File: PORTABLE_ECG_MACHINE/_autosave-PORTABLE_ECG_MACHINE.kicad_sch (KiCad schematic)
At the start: 55 parts, among them IC1 AD8232ACPZ, J1 USB_B_Micro, J2 Li-Ion 3.7 CONN, J3 UART, Q1 BSS138, Q2 BSS138, SW1 SW_SPDT, U1 CP2102-GM, U2 TP4056, U3 TC1262-33, U4 SSD1306

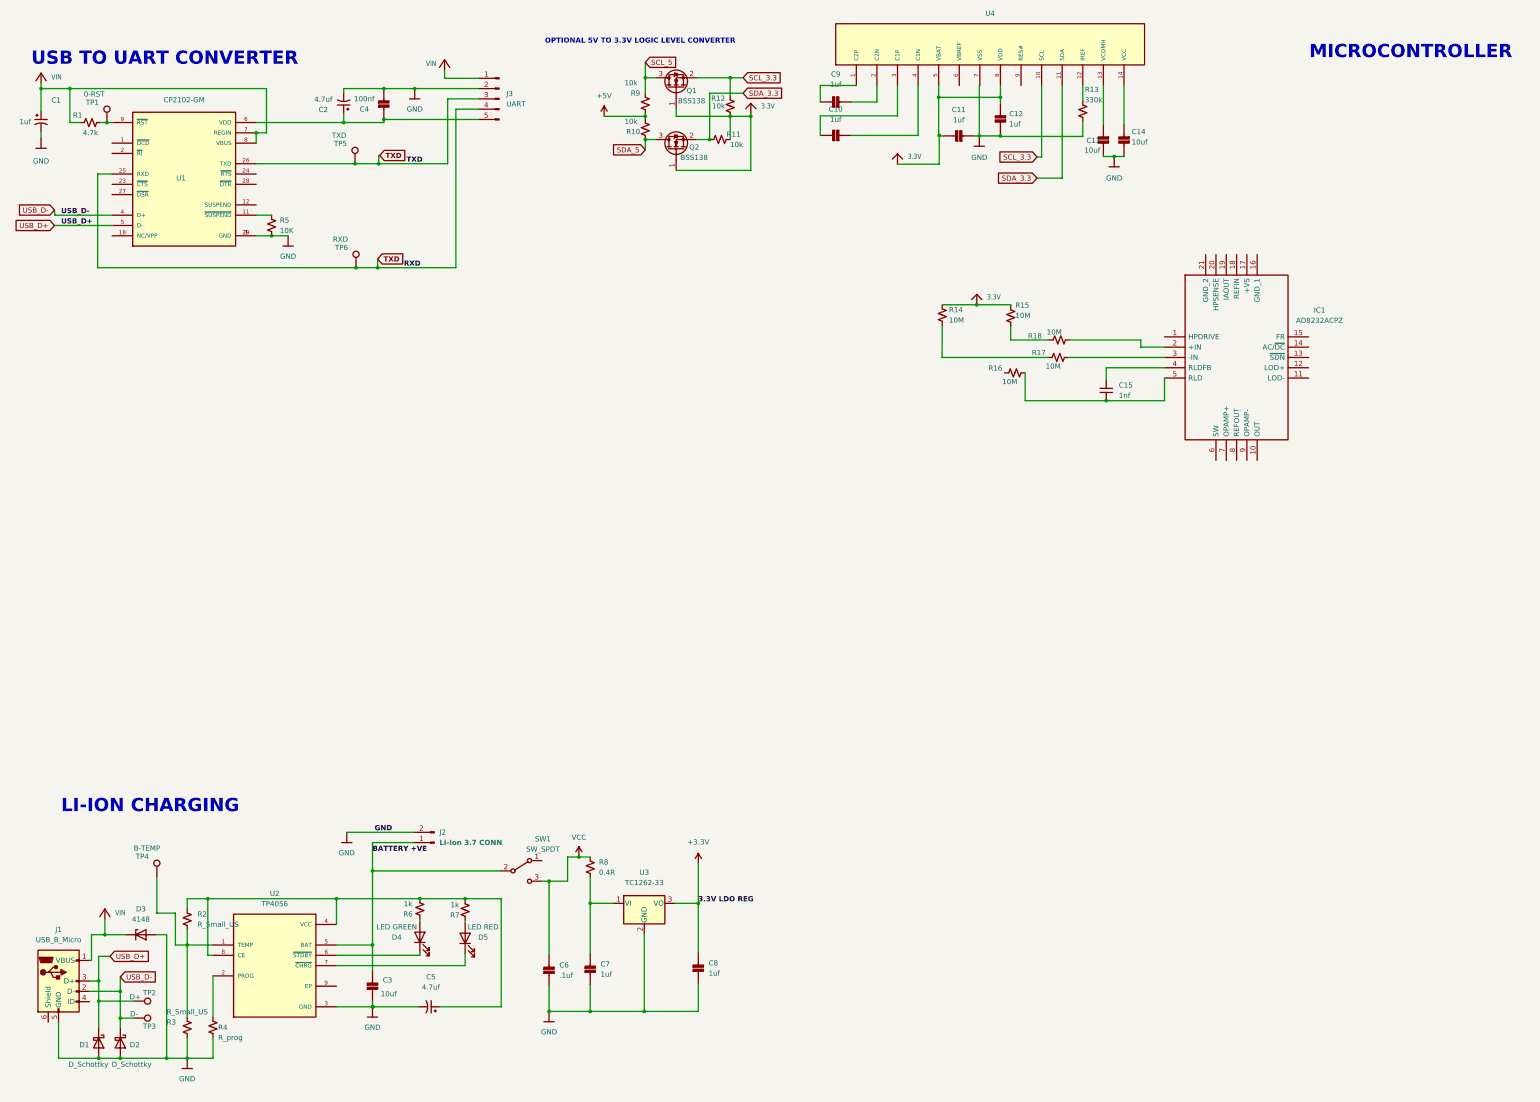
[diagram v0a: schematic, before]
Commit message: OLED-INSTR_AMP-LION_CHAR-UART EESCHEMA UPDATE | PCBNEW ROUGH ARANGE
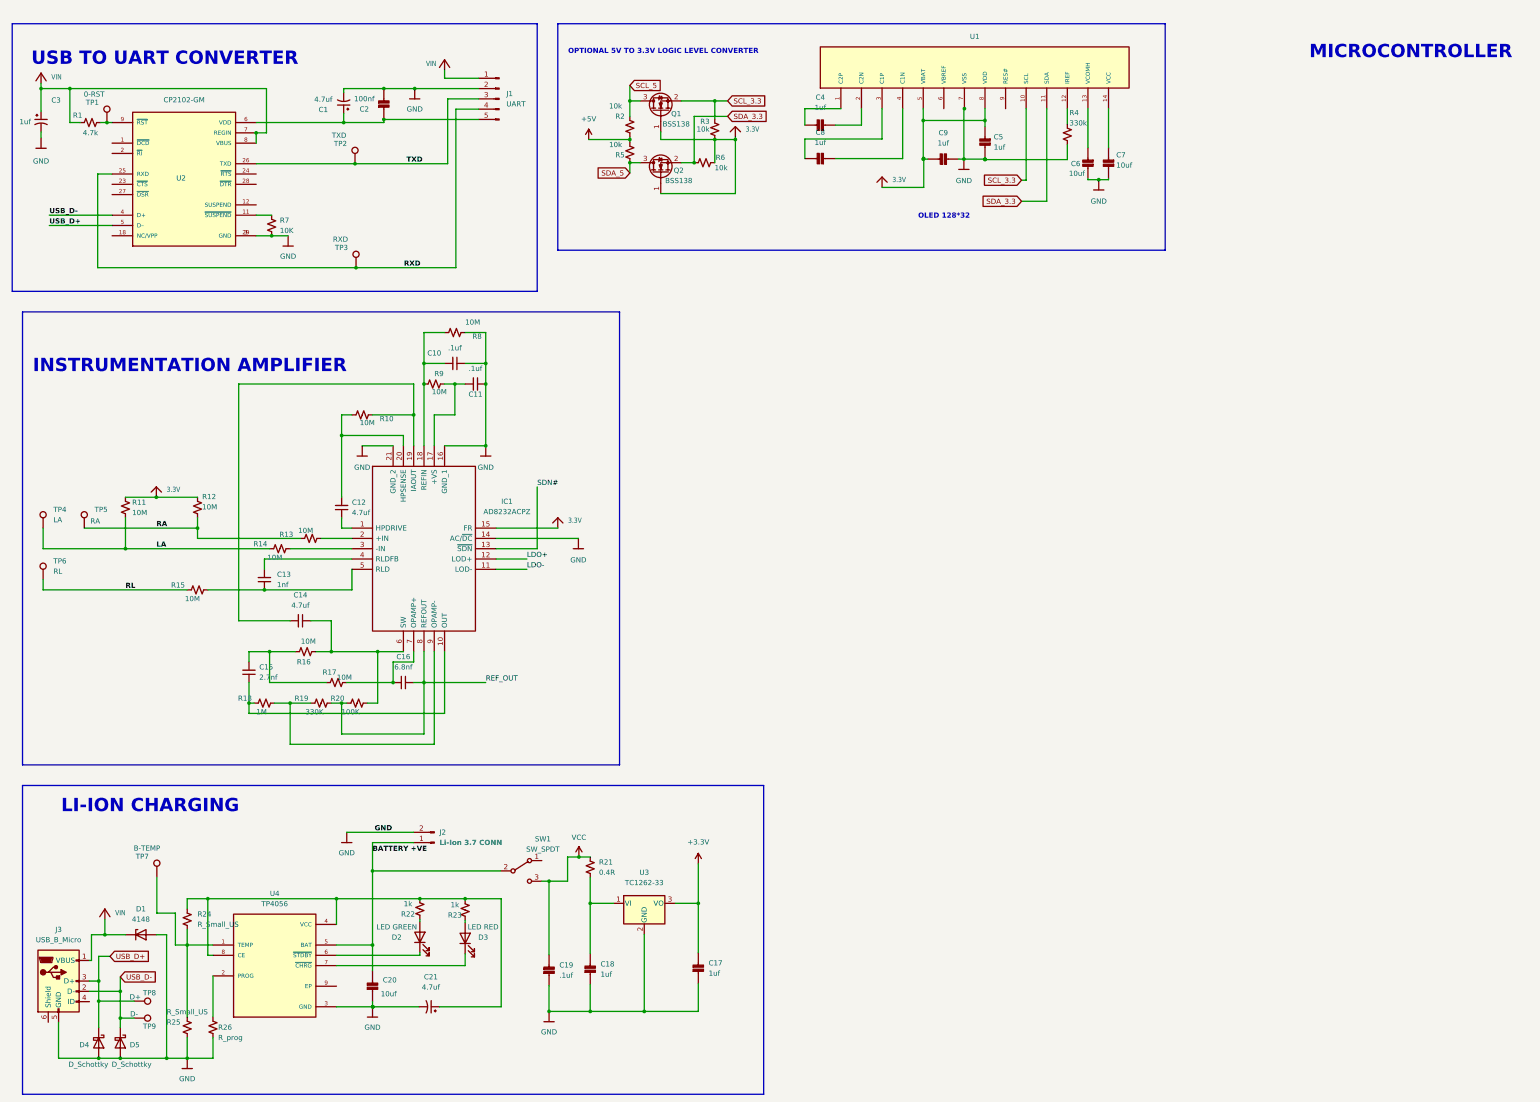
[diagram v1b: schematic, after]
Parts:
- added C10, C11: .1uf, Capacitor_SMD:C_0603_1608Metric, symbol Device:C_Small
- added C12, C14: 4.7uf, Capacitor_SMD:C_0603_1608Metric, symbol Device:C_Small
- added C15: 2.7nf, Capacitor_SMD:C_0603_1608Metric, symbol Device:C_Small
- added C16: 6.8nf, Capacitor_SMD:C_0603_1608Metric, symbol Device:C_Small
- added R10, R16, R17, R8, R9: 10M, Resistor_SMD:R_0603_1608Metric, symbol Device:R_Small_US
- added R18: 1M, Resistor_SMD:R_0603_1608Metric, symbol Device:R_Small_US
- added R19: 330K, Resistor_SMD:R_0603_1608Metric, symbol Device:R_Small_US
- added R20: 100K, Resistor_SMD:R_0603_1608Metric, symbol Device:R_Small_US
- added TP4: LA, TestPoint:TestPoint_Pad_D1.0mm, symbol Connector:TestPoint
- added TP5: RA, TestPoint:TestPoint_Pad_D1.0mm, symbol Connector:TestPoint
- added TP6: RL, TestPoint:TestPoint_Pad_D1.0mm, symbol Connector:TestPoint
- U4: renamed from U2; footprint SOP127P600X175-9N -> Package_TO_SOT_SMD:TSOT-23-8
- renumbered C2 to C1, C15 to C13, C8 to C17, C7 to C18, C6 to C19, C4 to C2, C3 to C20, C5 to C21, C1 to C3, C9 to C4, C12 to C5, C13 to C6, C14 to C7, C10 to C8, C11 to C9, D3 to D1, D4 to D2, D5 to D3, D1 to D4, D2 to D5, J3 to J1, J1 to J3, R14 to R11, R15 to R12, R18 to R13, R17 to R14, R16 to R15, R9 to R2, R8 to R21, R6 to R22, R7 to R23, R2 to R24, R3 to R25, R4 to R26, R12 to R3, R13 to R4, R10 to R5, R11 to R6, R5 to R7, TP5 to TP2, TP6 to TP3, TP4 to TP7, TP2 to TP8, TP3 to TP9, U4 to U1, U1 to U2
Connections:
- net 3.3V: now also IC1.15 (FR)
- net GND: now also IC1.14 (AC/~{DC}), IC1.16 (GND_1), IC1.21 (GND_2), C10.1, C11.1, R8.1
- net TXD: no longer J1.4 (Pin_4), TP3.1, U2.25 (RXD)
- net LA: now reaches R11.2, R14.1
- net LA: now also TP4.1
- net at IC1.1 (HPDRIVE): now also C12.1
- net at IC1.10 (OUT): now also C15.1, R18.1
- net LDO-: now reaches IC1.11 (LOD-)
- net LDO+: now reaches IC1.12 (LOD+)
- net SDN#: now reaches IC1.13 (~{SDN})
- net at IC1.17 (+VS): now also C11.2, R9.1
- net at IC1.18 (REFIN): now also C10.2, R8.2, R9.2
- net at IC1.19 (IAOUT): now also C14.2, R10.1
- net at IC1.20 (HPSENSE): now also C12.2, R10.2
- net at IC1.6 (SW): now also C14.1, R16.2, R20.2
- net at IC1.7 (OPAMP+): now also C16.2, R17.2
- net REF_OUT: now reaches IC1.8 (REFOUT)
- net REF_OUT: now also C16.1, R19.2, R20.1
- net at IC1.9 (OPAMP-): now also R18.2, R19.1
- net RL: now reaches R15.1
- net RL: now also TP6.1
- net RA: now reaches R12.2, R13.1
- net RA: now also TP5.1
- new net: C15.2, R16.1, R17.1
- new net RXD: J1.4 (Pin_4), TP3.1, U2.25 (RXD)
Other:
- note added: "INSTRUMENTATION AMPLIFIER"
- note added: "OLED 128*32"
- moved on the sheet: C13, C4, C5, C6, C7, C8, C9, IC1, Q1, Q2, R11, R12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
